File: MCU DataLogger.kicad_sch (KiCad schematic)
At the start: 25 parts, among them U1 24LC1025, U2 DS1337S_, U3 24LC1025, U4 ATMEGA328P-AU, Y1 32.768 KH, Y2 16MHz

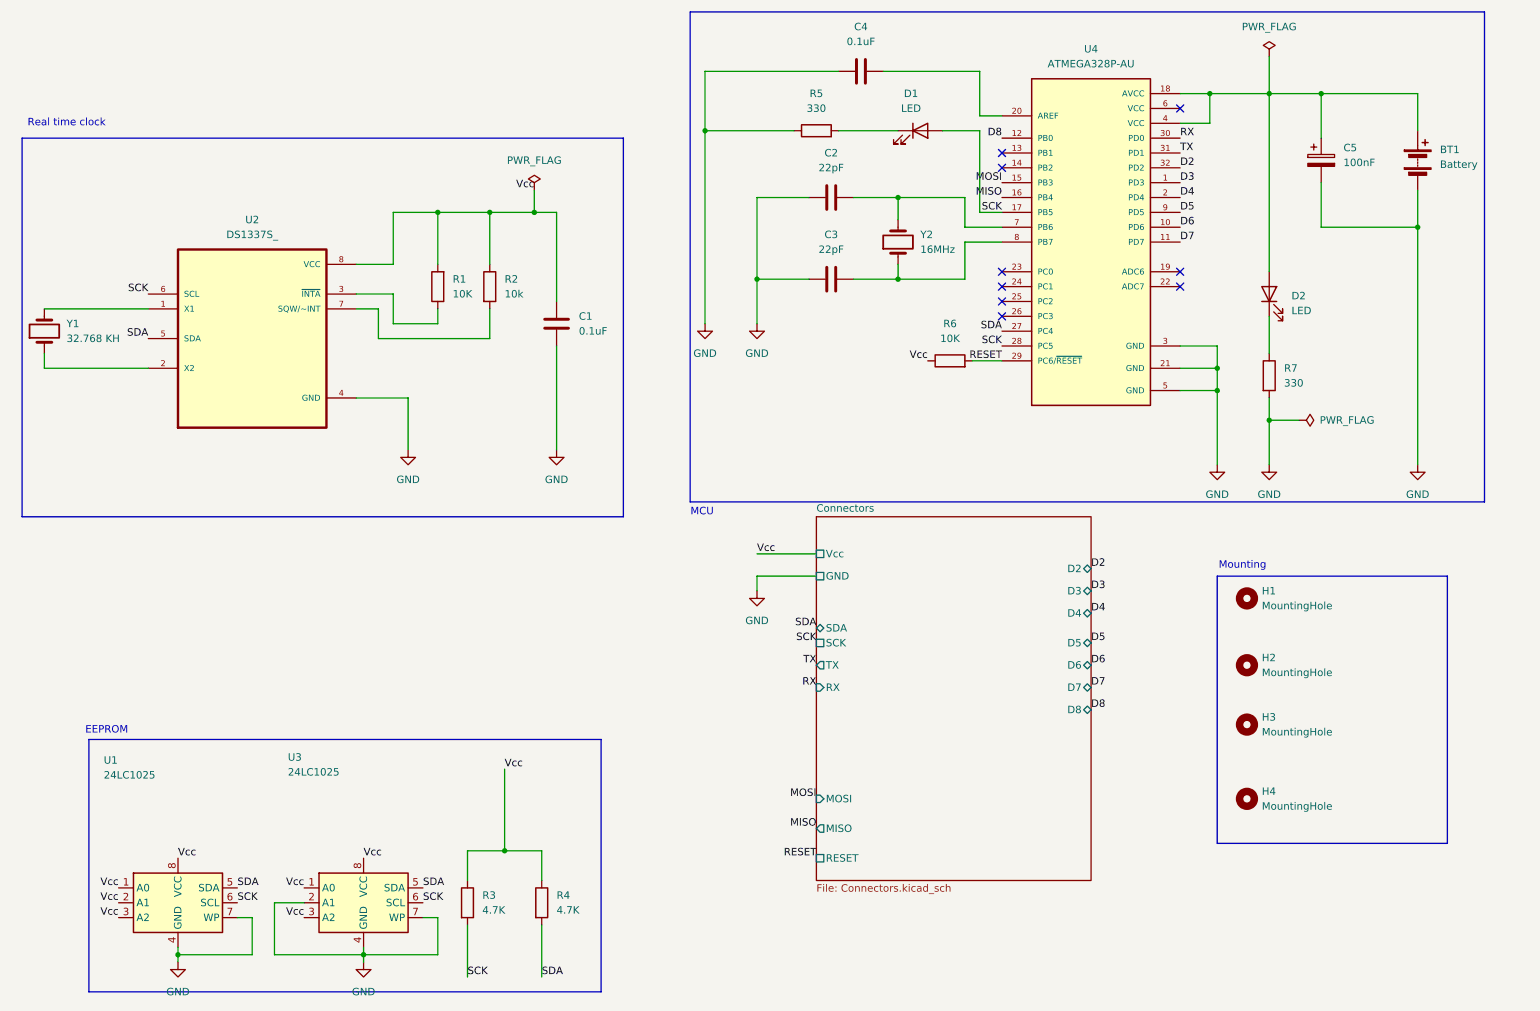
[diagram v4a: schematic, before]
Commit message: fixed shematic errors SCL vs SCK
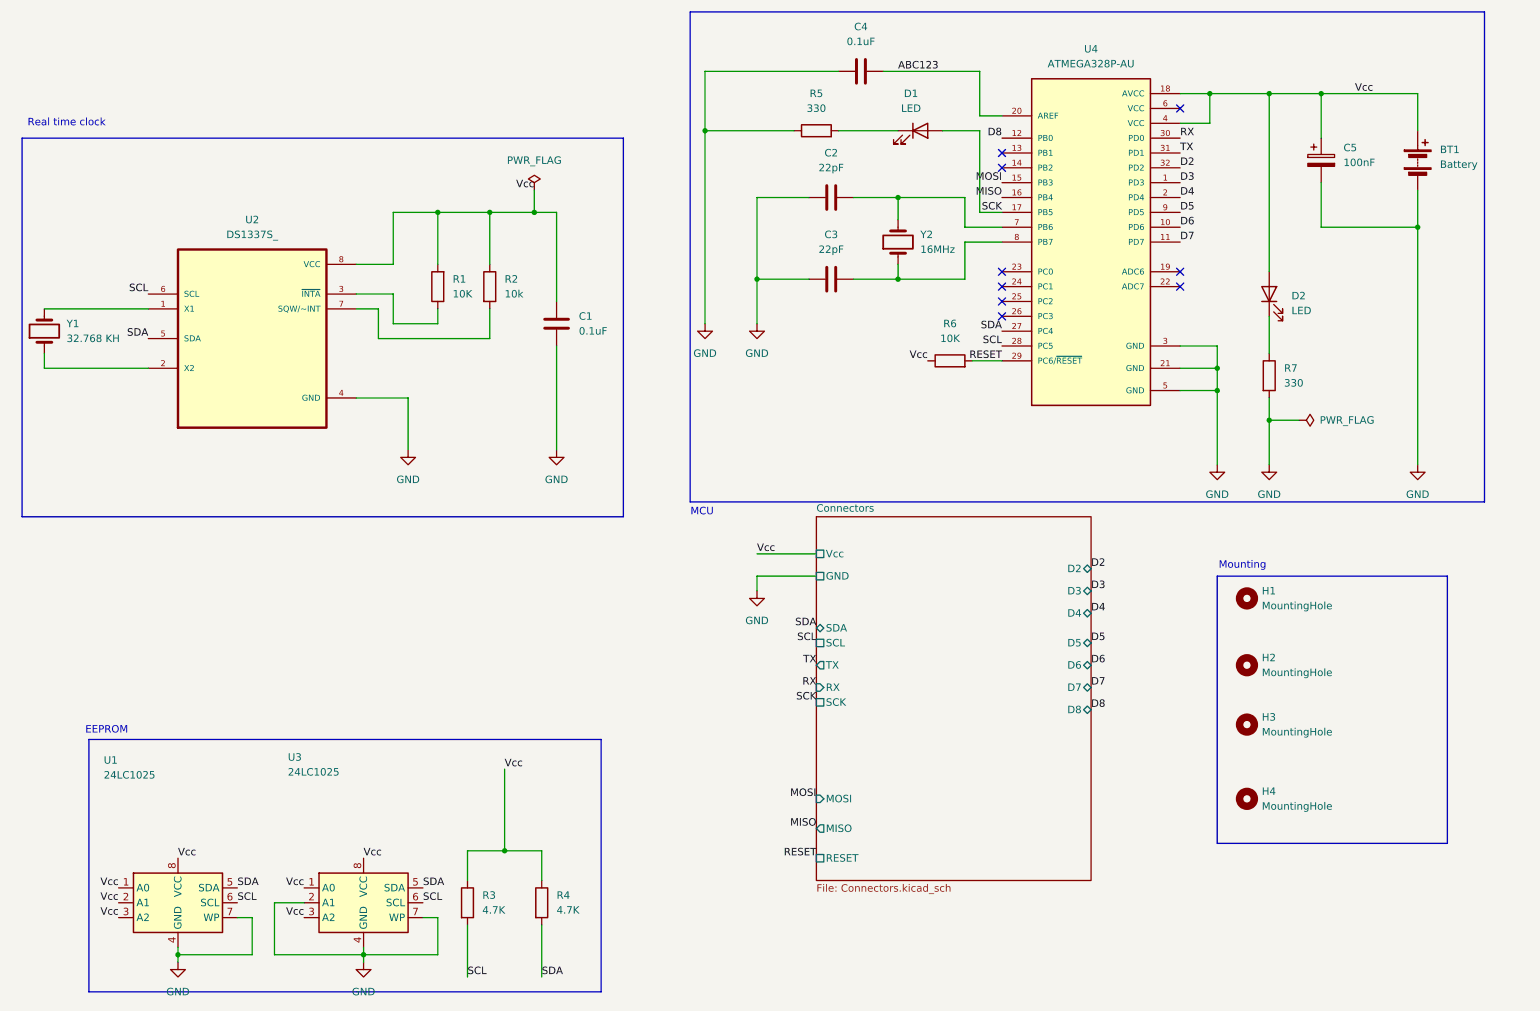
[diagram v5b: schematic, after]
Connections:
- net SCK: no longer R3.2, U1.6 (SCL), U2.6 (SCL), U3.6 (SCL), U4.28 (PC5)
- net Vcc: now also BT1.1 (+), C5.1, D2.2 (A), U4.18 (AVCC), U4.4 (VCC)
- net ABC123: now reaches C4.2, U4.20 (AREF)
- new net SCL: R3.2, U1.6 (SCL), U2.6 (SCL), U3.6 (SCL), U4.28 (PC5)
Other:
- sheet Connectors ports: added SCL; removed none
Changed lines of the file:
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@@
 	(wire
 		(pts
-			(xy 236.22 20.32) (xy 236.22 26.67)
-		)
-		(stroke
-			(width 0)
-			(type default)
-		)
-	)
-	(wire
-		(pts
 			(xy 93.98 167.64) (xy 93.98 173.99)
 		)
@@
 		)
 	)
+	(label "SCL"
+		(at 99.06 177.8 0)
+		(effects
+			(font
+				(size 1.27 1.27)
+			)
+			(justify left bottom)
+		)
+	)
 	(label "RESET"
 		(at 158.75 157.48 180)
@@
 		)
 	)
+	(label "SCL"
+		(at 59.69 165.1 0)
+		(effects
+			(font
+				(size 1.27 1.27)
+			)
+			(justify left bottom)
+		)
+	)
 	(label "Vcc"
 		(at 71.12 162.56 180)
@@
 		)
 	)
+	(label "SCL"
+		(at 91.44 165.1 0)
+		(effects
+			(font
+				(size 1.27 1.27)
+			)
+			(justify left bottom)
+		)
+	)
 	(label "SDA"
 		(at 111.76 177.8 0)
@@
 		)
 	)
-	(label "SCK"
-		(at 99.06 177.8 0)
+	(label "SCL"
+		(at 158.75 120.65 180)
 		(effects
 			(font
 				(size 1.27 1.27)
 			)
-			(justify left bottom)
+			(justify right bottom)
 		)
 	)
-	(label "SCK"
-		(at 59.69 165.1 0)
+	(label "SDA"
+		(at 59.69 162.56 0)
 		(effects
 			(font
@@
 	)
 	(label "SDA"
-		(at 59.69 162.56 0)
+		(at 190.5 67.31 180)
 		(effects
 			(font
 				(size 1.27 1.27)
 			)
-			(justify left bottom)
+			(justify right bottom)
 		)
 	)
-	(label "SDA"
-		(at 190.5 67.31 180)
+	(label "SCL"
+		(at 190.5 69.85 180)
 		(effects
 			(font
@@
 		)
 	)
-	(label "SCK"
-		(at 190.5 69.85 180)
+	(label "Vcc"
+		(at 254 26.67 180)
 		(effects
 			(font
@@
 		)
 	)
+	(label "ABC123"
+		(at 172.72 22.86 0)
+		(effects
+			(font
+				(size 1.27 1.27)
+			)
+			(justify left bottom)
+		)
+	)
 	(label "TX"
 		(at 158.75 124.46 180)
@@
 		)
 	)
-	(label "D8"
-		(at 205.74 132.08 0)
+	(label "SCL"
+		(at 44.45 60.96 180)
 		(effects
 			(font
 				(size 1.27 1.27)
 			)
-			(justify left bottom)
+			(justify right bottom)
 		)
 	)
-	(label "SCK"
-		(at 158.75 120.65 180)
+	(label "D8"
+		(at 205.74 132.08 0)
 		(effects
 			(font
 				(size 1.27 1.27)
 			)
-			(justify right bottom)
+			(justify left bottom)
 		)
 	)
@@
 		)
 	)
-	(label "SCK"
-		(at 44.45 60.96 180)
-		(effects
-			(font
-				(size 1.27 1.27)
-			)
-			(justify right bottom)
-		)
-	)
 	(label "D7"
 		(at 220.98 52.07 0)
@@
 		)
 	)
-	(label "MOSI"
-		(at 158.75 147.32 180)
+	(label "SCK"
+		(at 158.75 130.81 180)
 		(effects
 			(font
@@
 		)
 	)
-	(label "SCK"
-		(at 91.44 165.1 0)
+	(label "MOSI"
+		(at 158.75 147.32 180)
 		(effects
 			(font
 				(size 1.27 1.27)
 			)
-			(justify left bottom)
+			(justify right bottom)
 		)
 	)
@@
 		)
 	)
-	(symbol
-		(lib_id "power:PWR_FLAG")
-		(at 236.22 20.32 0)
-		(unit 1)
-		(body_style 1)
-		(exclude_from_sim no)
-		(in_bom yes)
-		(on_board yes)
-		(in_pos_files yes)
-		(dnp no)
-		(fields_autoplaced yes)
-		(property "Reference" "#FLG02"
-			(at 236.22 18.415 0)
-			(hide yes)
-			(show_name no)
-			(do_not_autoplace no)
-			(effects
-				(font
-					(size 1.27 1.27)
-				)
-			)
-		)
-		(property "Value" "PWR_FLAG"
-			(at 236.22 15.24 0)
-			(show_name no)
-			(do_not_autoplace no)
-			(effects
-				(font
-					(size 1.27 1.27)
-				)
-			)
-		)
-		(property "Footprint" ""
-			(at 236.22 20.32 0)
-			(hide yes)
-			(show_name no)
-			(do_not_autoplace no)
-			(effects
-				(font
-					(size 1.27 1.27)
-				)
-			)
-		)
-		(property "Datasheet" ""
-			(at 236.22 20.32 0)
-			(hide yes)
-			(show_name no)
-			(do_not_autoplace no)
-			(effects
-				(font
-					(size 1.27 1.27)
-				)
-			)
-		)
-		(property "Description" "Special symbol for telling ERC where power comes from"
-			(at 236.22 20.32 0)
-			(hide yes)
-			(show_name no)
-			(do_not_autoplace no)
-			(effects
-				(font
-					(size 1.27 1.27)
-				)
-			)
-		)
-		(pin "1"
-		)
-		(instances
-			(project "MCU Datalogger"
-				(path "/82352dda-4ca1-40c9-b7a4-aaa22a39ffc1"
-					(reference "#FLG02")
-					(unit 1)
-				)
-			)
-		)
-	)
 	(sheet
 		(at 158.75 99.06)
@@
 			)
 		)
-		(pin "SCK" passive
-			(at 158.75 120.65 180)
+		(pin "SDA" bidirectional
+			(at 158.75 118.11 180)
 			(effects
 				(font
@@
 			)
 		)
-		(pin "SDA" bidirectional
-			(at 158.75 118.11 180)
+		(pin "TX" output
+			(at 158.75 124.46 180)
 			(effects
 				(font
@@
 			)
 		)
-		(pin "TX" output
-			(at 158.75 124.46 180)
+		(pin "Vcc" passive
+			(at 158.75 105.41 180)
 			(effects
 				(font
@@
 			)
 		)
-		(pin "Vcc" passive
-			(at 158.75 105.41 180)
+		(pin "SCK" passive
+			(at 158.75 130.81 180)
+			(effects
+				(font
+					(size 1.27 1.27)
+				)
+				(justify left)
+			)
+		)
+		(pin "SCL" passive
+			(at 158.75 120.65 180)
 			(effects
 				(font
